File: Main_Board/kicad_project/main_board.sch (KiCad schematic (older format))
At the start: 0 parts

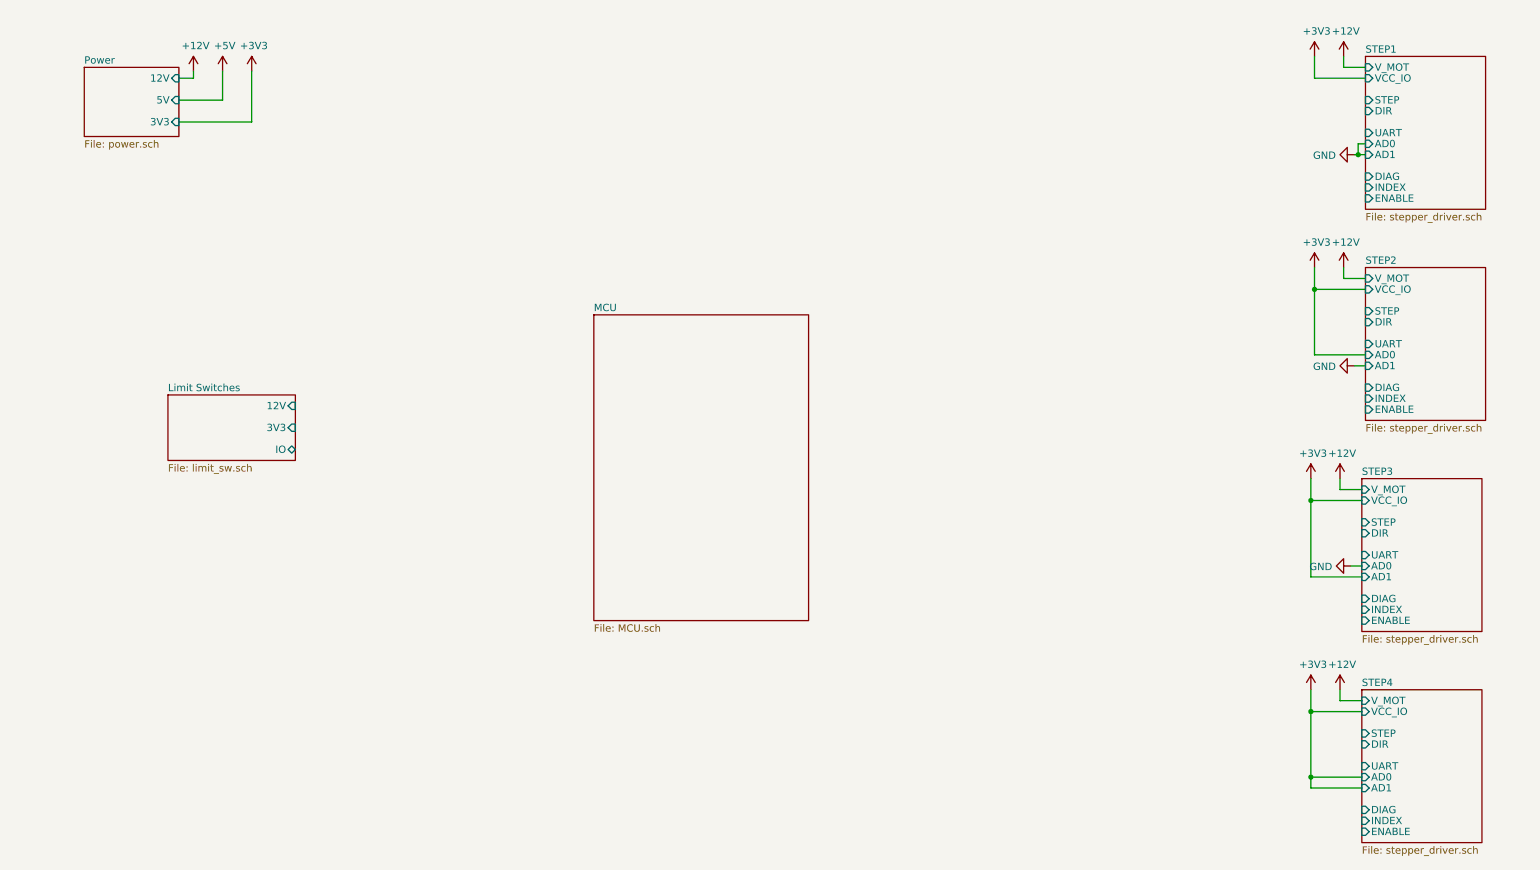
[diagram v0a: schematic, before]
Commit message: add external IO
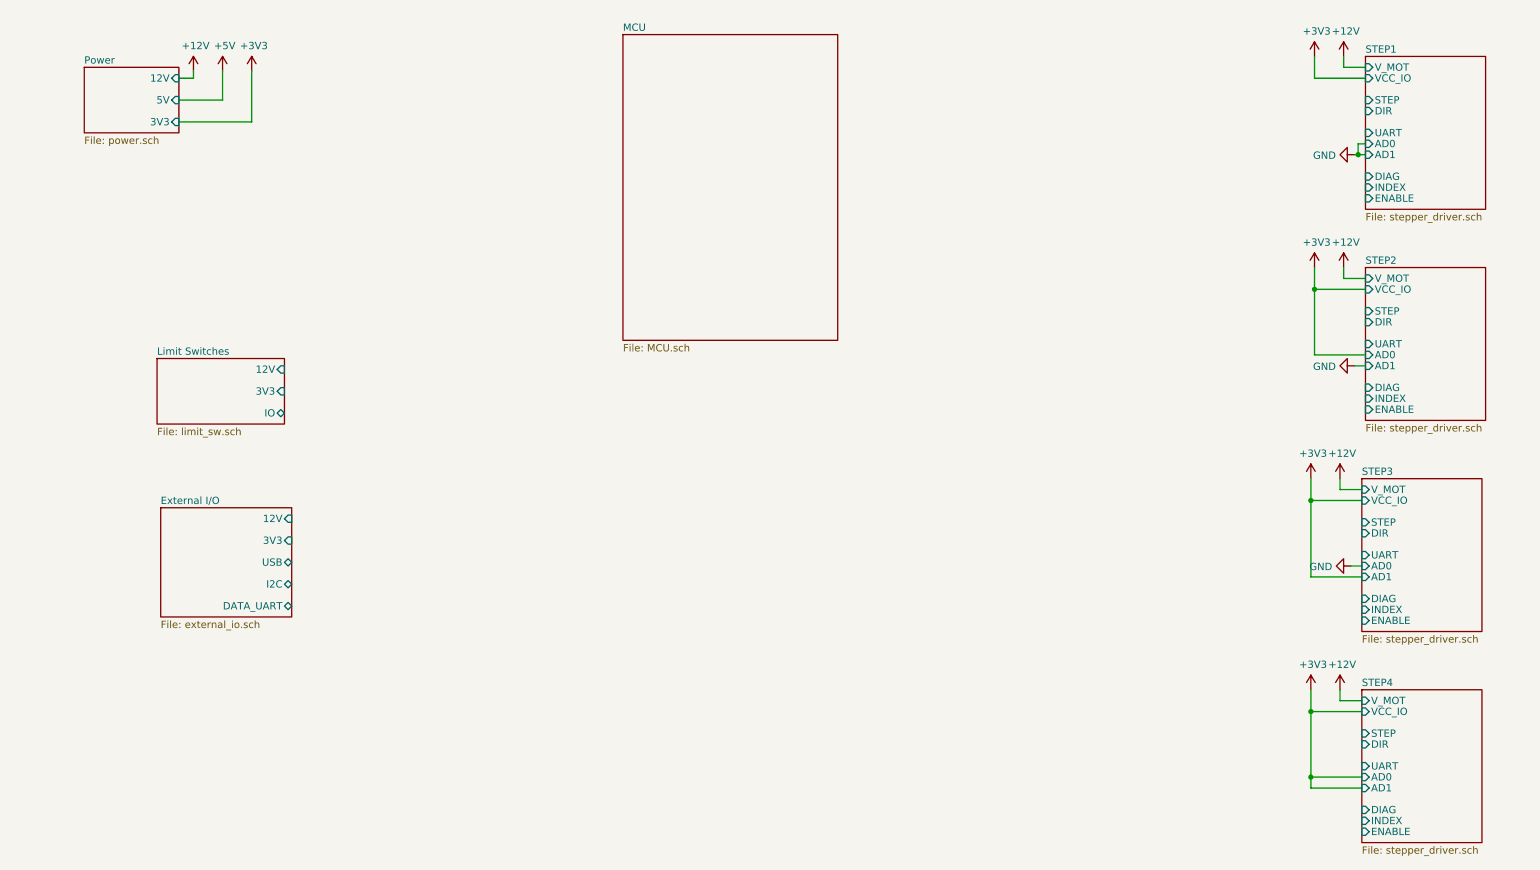
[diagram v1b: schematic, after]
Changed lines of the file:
@@
 $Descr A4 11693 8268
 encoding utf-8
-Sheet 1 8
+Sheet 1 9
 Title "Cube Main Board - top level schematic"
 Date ""
@@
 $EndComp
 $Sheet
-S 1050 925  650  475
+S 1050 925  650  450
 U 5F4D5F3E
 F0 "Power" 50
@@
 $EndComp
 $Sheet
-S 4550 2625 1475 2100
+S 4750 700  1475 2100
 U 5F5463C2
 F0 "MCU" 50
@@
 $EndSheet
 $Sheet
-S 1625 3175 875  450
+S 1550 2925 875  450
 U 5F51A37F
 F0 "Limit Switches" 50
 F1 "limit_sw.sch" 50
-F2 "3V3" I R 2500 3400 50
-F3 "12V" I R 2500 3250 50
-F4 "IO" B R 2500 3550 50
+F2 "3V3" I R 2425 3150 50
+F3 "12V" I R 2425 3000 50
+F4 "IO" B R 2425 3300 50
+$EndSheet
+$Sheet
+S 1575 3950 900  750
+U 5F709561
+F0 "External I/O" 50
+F1 "external_io.sch" 50
+F2 "USB" B R 2475 4325 50
+F3 "3V3" I R 2475 4175 50
+F4 "12V" I R 2475 4025 50
+F5 "I2C" B R 2475 4475 50
+F6 "DATA_UART" B R 2475 4625 50
 $EndSheet
 $EndSCHEMATC

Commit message: progress?
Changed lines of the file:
@@
 	9500 1000 9500 850
 $Comp
-L power:+3V3 #PWR?
+L power:+3V3 #PWR06
 U 1 1 5F4AAFEB
 P 9500 850
-F 0 "#PWR?" H 9500 700 50  0001 C CNN
+F 0 "#PWR06" H 9500 700 50  0001 C CNN
 F 1 "+3V3" H 9515 1023 50  0000 C CNN
 F 2 "" H 9500 850 50  0001 C CNN
@@
 	9500 2450 9500 2300
 $Comp
-L power:+3V3 #PWR?
+L power:+3V3 #PWR07
 U 1 1 5F4AC7A4
 P 9500 2300
-F 0 "#PWR?" H 9500 2150 50  0001 C CNN
+F 0 "#PWR07" H 9500 2150 50  0001 C CNN
 F 1 "+3V3" H 9515 2473 50  0000 C CNN
 F 2 "" H 9500 2300 50  0001 C CNN
@@
 	9475 3900 9475 3750
 $Comp
-L power:+3V3 #PWR?
+L power:+3V3 #PWR04
 U 1 1 5F4AD226
 P 9475 3750
-F 0 "#PWR?" H 9475 3600 50  0001 C CNN
+F 0 "#PWR04" H 9475 3600 50  0001 C CNN
 F 1 "+3V3" H 9490 3923 50  0000 C CNN
 F 2 "" H 9475 3750 50  0001 C CNN
@@
 	9475 5350 9475 5200
 $Comp
-L power:+3V3 #PWR?
+L power:+3V3 #PWR05
 U 1 1 5F4ADFB4
 P 9475 5200
-F 0 "#PWR?" H 9475 5050 50  0001 C CNN
+F 0 "#PWR05" H 9475 5050 50  0001 C CNN
 F 1 "+3V3" H 9490 5373 50  0000 C CNN
 F 2 "" H 9475 5200 50  0001 C CNN
@@
 $EndComp
 $Sheet
-S 1050 925  650  450
+S 1200 925  650  450
 U 5F4D5F3E
 F0 "Power" 50
 F1 "power.sch" 50
-F2 "3V3" I R 1700 1300 50
-F3 "12V" I R 1700 1000 50
-F4 "5V" I R 1700 1150 50
-$EndSheet
-$Comp
-L power:+12V #PWR?
+F2 "3V3" I R 1850 1300 50
+F3 "12V" I R 1850 1000 50
+F4 "5V" I R 1850 1150 50
+$EndSheet
+$Comp
+L power:+12V #PWR09
 U 1 1 5F5780D9
 P 9675 5200
-F 0 "#PWR?" H 9675 5050 50  0001 C CNN
+F 0 "#PWR09" H 9675 5050 50  0001 C CNN
 F 1 "+12V" H 9690 5373 50  0000 C CNN
 F 2 "" H 9675 5200 50  0001 C CNN
@@
 $EndComp
 $Comp
-L power:+12V #PWR?
+L power:+12V #PWR08
 U 1 1 5F578445
 P 9675 3750
-F 0 "#PWR?" H 9675 3600 50  0001 C CNN
+F 0 "#PWR08" H 9675 3600 50  0001 C CNN
 F 1 "+12V" H 9690 3923 50  0000 C CNN
 F 2 "" H 9675 3750 50  0001 C CNN
@@
 $EndComp
 $Comp
-L power:+12V #PWR?
+L power:+12V #PWR011
 U 1 1 5F578DCD
 P 9700 2300
-F 0 "#PWR?" H 9700 2150 50  0001 C CNN
+F 0 "#PWR011" H 9700 2150 50  0001 C CNN
 F 1 "+12V" H 9715 2473 50  0000 C CNN
 F 2 "" H 9700 2300 50  0001 C CNN
@@
 $EndComp
 $Comp
-L power:+12V #PWR?
+L power:+12V #PWR010
 U 1 1 5F579C0A
 P 9700 850
-F 0 "#PWR?" H 9700 700 50  0001 C CNN
+F 0 "#PWR010" H 9700 700 50  0001 C CNN
 F 1 "+12V" H 9715 1023 50  0000 C CNN
 F 2 "" H 9700 850 50  0001 C CNN
@@
 $EndComp
 $Comp
-L power:+12V #PWR?
+L power:+12V #PWR01
 U 1 1 5F634CDC
-P 1800 950
-F 0 "#PWR?" H 1800 800 50  0001 C CNN
-F 1 "+12V" H 1815 1123 50  0000 C CNN
-F 2 "" H 1800 950 50  0001 C CNN
-F 3 "" H 1800 950 50  0001 C CNN
-	1    1800 950
-	1    0    0    -1
-$EndComp
-$Comp
-L power:+3V3 #PWR?
+P 1950 950
+F 0 "#PWR01" H 1950 800 50  0001 C CNN
+F 1 "+12V" H 1965 1123 50  0000 C CNN
+F 2 "" H 1950 950 50  0001 C CNN
+F 3 "" H 1950 950 50  0001 C CNN
+	1    1950 950
+	1    0    0    -1
+$EndComp
+$Comp
+L power:+3V3 #PWR03
 U 1 1 5F635D56
-P 2200 950
-F 0 "#PWR?" H 2200 800 50  0001 C CNN
-F 1 "+3V3" H 2215 1123 50  0000 C CNN
-F 2 "" H 2200 950 50  0001 C CNN
-F 3 "" H 2200 950 50  0001 C CNN
-	1    2200 950
-	1    0    0    -1
-$EndComp
-$Comp
-L power:+5V #PWR?
+P 2350 950
+F 0 "#PWR03" H 2350 800 50  0001 C CNN
+F 1 "+3V3" H 2365 1123 50  0000 C CNN
+F 2 "" H 2350 950 50  0001 C CNN
+F 3 "" H 2350 950 50  0001 C CNN
+	1    2350 950
+	1    0    0    -1
+$EndComp
+$Comp
+L power:+5V #PWR02
 U 1 1 5F636812
-P 2000 950
-F 0 "#PWR?" H 2000 800 50  0001 C CNN
-F 1 "+5V" H 2015 1123 50  0000 C CNN
-F 2 "" H 2000 950 50  0001 C CNN
-F 3 "" H 2000 950 50  0001 C CNN
-	1    2000 950
-	1    0    0    -1
-$EndComp
-Wire Wire Line
-	2200 950  2200 1300
-Wire Wire Line
-	2200 1300 1700 1300
-Wire Wire Line
-	1700 1150 2000 1150
-Wire Wire Line
-	2000 1150 2000 950
-Wire Wire Line
-	1700 1000 1800 1000
-Wire Wire Line
-	1800 1000 1800 950
+P 2150 950
+F 0 "#PWR02" H 2150 800 50  0001 C CNN
+F 1 "+5V" H 2165 1123 50  0000 C CNN
+F 2 "" H 2150 950 50  0001 C CNN
+F 3 "" H 2150 950 50  0001 C CNN
+	1    2150 950
+	1    0    0    -1
+$EndComp
+Wire Wire Line
+	2350 950  2350 1300
+Wire Wire Line
+	2350 1300 1850 1300
+Wire Wire Line
+	1850 1150 2150 1150
+Wire Wire Line
+	2150 1150 2150 950
+Wire Wire Line
+	1850 1000 1950 1000
+Wire Wire Line
+	1950 1000 1950 950
 Wire Wire Line
 	9825 4425 9475 4425
@@
 Connection ~ 9475 5800
 $Comp
-L power:GND #PWR?
+L power:GND #PWR013
 U 1 1 5F537589
 P 9775 1525
-F 0 "#PWR?" H 9775 1275 50  0001 C CNN
+F 0 "#PWR013" H 9775 1275 50  0001 C CNN
 F 1 "GND" V 9780 1397 50  0000 R CNN
 F 2 "" H 9775 1525 50  0001 C CNN
@@
 $EndComp
 $Comp
-L power:GND #PWR?
+L power:GND #PWR014
 U 1 1 5F53878C
 P 9775 2975
-F 0 "#PWR?" H 9775 2725 50  0001 C CNN
+F 0 "#PWR014" H 9775 2725 50  0001 C CNN
 F 1 "GND" V 9780 2847 50  0000 R CNN
 F 2 "" H 9775 2975 50  0001 C CNN
@@
 	9500 2900 9500 2450
 $Comp
-L power:GND #PWR?
+L power:GND #PWR012
 U 1 1 5F5393A9
 P 9750 4350
-F 0 "#PWR?" H 9750 4100 50  0001 C CNN
+F 0 "#PWR012" H 9750 4100 50  0001 C CNN
 F 1 "GND" V 9755 4222 50  0000 R CNN
 F 2 "" H 9750 4350 50  0001 C CNN
@@
 $EndComp
 $Sheet
-S 4750 700  1475 2100
+S 5225 2475 1475 2100
 U 5F5463C2
 F0 "MCU" 50
 F1 "MCU.sch" 50
-$EndSheet
-$Sheet
-S 1550 2925 875  450
+F2 "VDD" I L 5225 2575 50
+F3 "VDDA" I L 5225 2700 50
+F4 "USB" B L 5225 3275 50
+$EndSheet
+$Sheet
+S 3000 2550 875  450
 U 5F51A37F
 F0 "Limit Switches" 50
 F1 "limit_sw.sch" 50
-F2 "3V3" I R 2425 3150 50
-F3 "12V" I R 2425 3000 50
-F4 "IO" B R 2425 3300 50
-$EndSheet
-$Sheet
-S 1575 3950 900  750
+F2 "3V3" I R 3875 2775 50
+F3 "12V" I R 3875 2625 50
+F4 "IO" B R 3875 2925 50
+$EndSheet
+$Sheet
+S 3000 3275 900  750
 U 5F709561
 F0 "External I/O" 50
 F1 "external_io.sch" 50
-F2 "USB" B R 2475 4325 50
-F3 "3V3" I R 2475 4175 50
-F4 "12V" I R 2475 4025 50
-F5 "I2C" B R 2475 4475 50
-F6 "DATA_UART" B R 2475 4625 50
-$EndSheet
+F2 "USB" B R 3900 3650 50
+F3 "3V3" I R 3900 3500 50
+F4 "12V" I R 3900 3350 50
+F5 "I2C" B R 3900 3800 50
+F6 "DATA_UART" B R 3900 3950 50
+$EndSheet
+Wire Bus Line
+	3900 3650 4550 3650
+Wire Bus Line
+	4550 3650 4550 3275
+Wire Bus Line
+	4550 3275 5225 3275
 $EndSCHEMATC

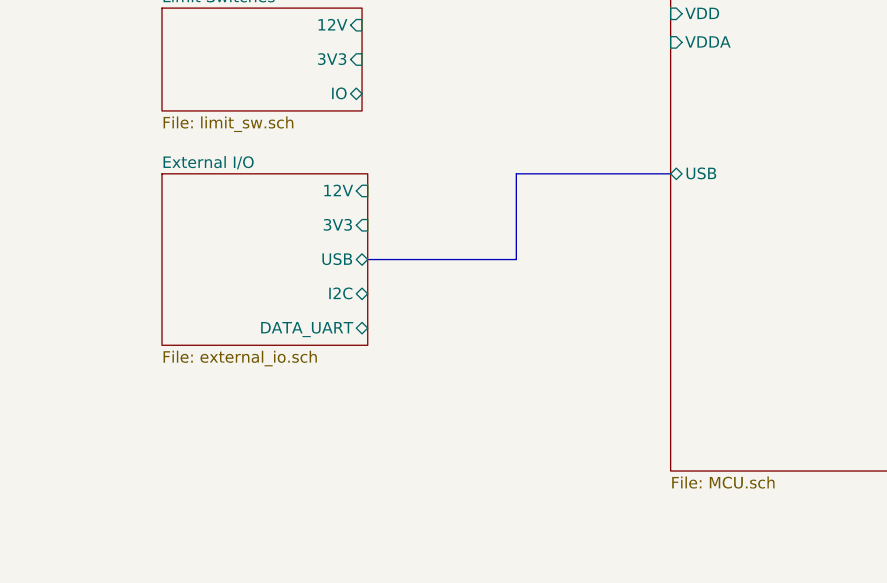
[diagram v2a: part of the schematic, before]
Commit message: progress on MCU pinout
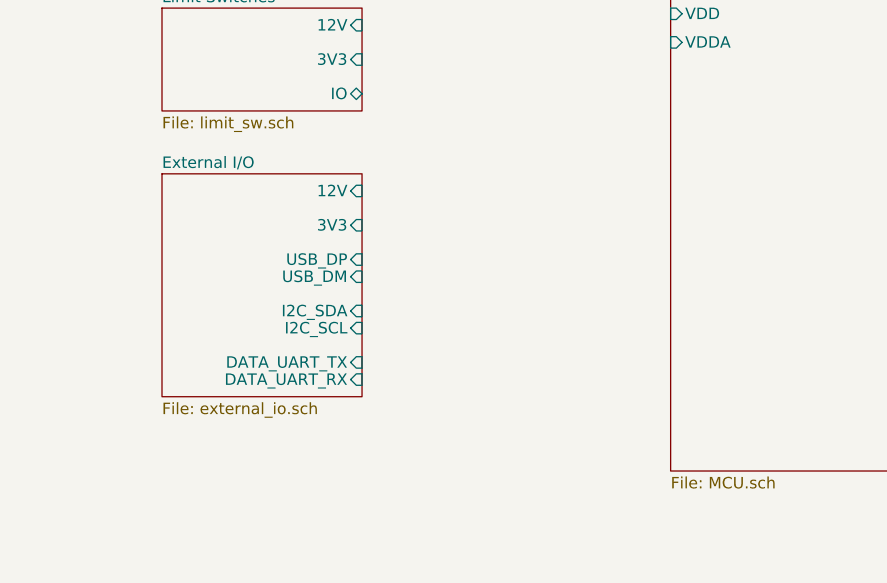
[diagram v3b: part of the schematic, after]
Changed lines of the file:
@@
 	9500 1000 9500 850
 $Comp
-L power:+3V3 #PWR06
+L power:+3V3 #PWR?
 U 1 1 5F4AAFEB
 P 9500 850
-F 0 "#PWR06" H 9500 700 50  0001 C CNN
+F 0 "#PWR?" H 9500 700 50  0001 C CNN
 F 1 "+3V3" H 9515 1023 50  0000 C CNN
 F 2 "" H 9500 850 50  0001 C CNN
@@
 	9500 2450 9500 2300
 $Comp
-L power:+3V3 #PWR07
+L power:+3V3 #PWR?
 U 1 1 5F4AC7A4
 P 9500 2300
-F 0 "#PWR07" H 9500 2150 50  0001 C CNN
+F 0 "#PWR?" H 9500 2150 50  0001 C CNN
 F 1 "+3V3" H 9515 2473 50  0000 C CNN
 F 2 "" H 9500 2300 50  0001 C CNN
@@
 	9475 3900 9475 3750
 $Comp
-L power:+3V3 #PWR04
+L power:+3V3 #PWR?
 U 1 1 5F4AD226
 P 9475 3750
-F 0 "#PWR04" H 9475 3600 50  0001 C CNN
+F 0 "#PWR?" H 9475 3600 50  0001 C CNN
 F 1 "+3V3" H 9490 3923 50  0000 C CNN
 F 2 "" H 9475 3750 50  0001 C CNN
@@
 	9475 5350 9475 5200
 $Comp
-L power:+3V3 #PWR05
+L power:+3V3 #PWR?
 U 1 1 5F4ADFB4
 P 9475 5200
-F 0 "#PWR05" H 9475 5050 50  0001 C CNN
+F 0 "#PWR?" H 9475 5050 50  0001 C CNN
 F 1 "+3V3" H 9490 5373 50  0000 C CNN
 F 2 "" H 9475 5200 50  0001 C CNN
@@
 $EndSheet
 $Comp
-L power:+12V #PWR09
+L power:+12V #PWR?
 U 1 1 5F5780D9
 P 9675 5200
-F 0 "#PWR09" H 9675 5050 50  0001 C CNN
+F 0 "#PWR?" H 9675 5050 50  0001 C CNN
 F 1 "+12V" H 9690 5373 50  0000 C CNN
 F 2 "" H 9675 5200 50  0001 C CNN
@@
 $EndComp
 $Comp
-L power:+12V #PWR08
+L power:+12V #PWR?
 U 1 1 5F578445
 P 9675 3750
-F 0 "#PWR08" H 9675 3600 50  0001 C CNN
+F 0 "#PWR?" H 9675 3600 50  0001 C CNN
 F 1 "+12V" H 9690 3923 50  0000 C CNN
 F 2 "" H 9675 3750 50  0001 C CNN
@@
 $EndComp
 $Comp
-L power:+12V #PWR011
+L power:+12V #PWR?
 U 1 1 5F578DCD
 P 9700 2300
-F 0 "#PWR011" H 9700 2150 50  0001 C CNN
+F 0 "#PWR?" H 9700 2150 50  0001 C CNN
 F 1 "+12V" H 9715 2473 50  0000 C CNN
 F 2 "" H 9700 2300 50  0001 C CNN
@@
 $EndComp
 $Comp
-L power:+12V #PWR010
+L power:+12V #PWR?
 U 1 1 5F579C0A
 P 9700 850
-F 0 "#PWR010" H 9700 700 50  0001 C CNN
+F 0 "#PWR?" H 9700 700 50  0001 C CNN
 F 1 "+12V" H 9715 1023 50  0000 C CNN
 F 2 "" H 9700 850 50  0001 C CNN
@@
 $EndComp
 $Comp
-L power:+12V #PWR01
+L power:+12V #PWR?
 U 1 1 5F634CDC
 P 1950 950
-F 0 "#PWR01" H 1950 800 50  0001 C CNN
+F 0 "#PWR?" H 1950 800 50  0001 C CNN
 F 1 "+12V" H 1965 1123 50  0000 C CNN
 F 2 "" H 1950 950 50  0001 C CNN
@@
 $EndComp
 $Comp
-L power:+3V3 #PWR03
+L power:+3V3 #PWR?
 U 1 1 5F635D56
 P 2350 950
-F 0 "#PWR03" H 2350 800 50  0001 C CNN
+F 0 "#PWR?" H 2350 800 50  0001 C CNN
 F 1 "+3V3" H 2365 1123 50  0000 C CNN
 F 2 "" H 2350 950 50  0001 C CNN
@@
 $EndComp
 $Comp
-L power:+5V #PWR02
+L power:+5V #PWR?
 U 1 1 5F636812
 P 2150 950
-F 0 "#PWR02" H 2150 800 50  0001 C CNN
+F 0 "#PWR?" H 2150 800 50  0001 C CNN
 F 1 "+5V" H 2165 1123 50  0000 C CNN
 F 2 "" H 2150 950 50  0001 C CNN
@@
 Connection ~ 9475 5800
 $Comp
-L power:GND #PWR013
+L power:GND #PWR?
 U 1 1 5F537589
 P 9775 1525
-F 0 "#PWR013" H 9775 1275 50  0001 C CNN
+F 0 "#PWR?" H 9775 1275 50  0001 C CNN
 F 1 "GND" V 9780 1397 50  0000 R CNN
 F 2 "" H 9775 1525 50  0001 C CNN
@@
 $EndComp
 $Comp
-L power:GND #PWR014
+L power:GND #PWR?
 U 1 1 5F53878C
 P 9775 2975
-F 0 "#PWR014" H 9775 2725 50  0001 C CNN
+F 0 "#PWR?" H 9775 2725 50  0001 C CNN
 F 1 "GND" V 9780 2847 50  0000 R CNN
 F 2 "" H 9775 2975 50  0001 C CNN
@@
 	9500 2900 9500 2450
 $Comp
-L power:GND #PWR012
+L power:GND #PWR?
 U 1 1 5F5393A9
 P 9750 4350
-F 0 "#PWR012" H 9750 4100 50  0001 C CNN
+F 0 "#PWR?" H 9750 4100 50  0001 C CNN
 F 1 "GND" V 9755 4222 50  0000 R CNN
 F 2 "" H 9750 4350 50  0001 C CNN
@@
 F2 "VDD" I L 5225 2575 50
 F3 "VDDA" I L 5225 2700 50
-F4 "USB" B L 5225 3275 50
 $EndSheet
 $Sheet
@@
 $EndSheet
 $Sheet
-S 3000 3275 900  750
+S 3000 3275 875  975
 U 5F709561
 F0 "External I/O" 50
 F1 "external_io.sch" 50
-F2 "USB" B R 3900 3650 50
-F3 "3V3" I R 3900 3500 50
-F4 "12V" I R 3900 3350 50
-F5 "I2C" B R 3900 3800 50
-F6 "DATA_UART" B R 3900 3950 50
-$EndSheet
-Wire Bus Line
-	3900 3650 4550 3650
-Wire Bus Line
-	4550 3650 4550 3275
-Wire Bus Line
-	4550 3275 5225 3275
+F2 "3V3" I R 3875 3500 50
+F3 "12V" I R 3875 3350 50
+F4 "USB_DP" I R 3875 3650 50
+F5 "USB_DM" I R 3875 3725 50
+F6 "I2C_SDA" I R 3875 3875 50
+F7 "I2C_SCL" I R 3875 3950 50
+F8 "DATA_UART_TX" I R 3875 4100 50
+F9 "DATA_UART_RX" I R 3875 4175 50
+$EndSheet
 $EndSCHEMATC

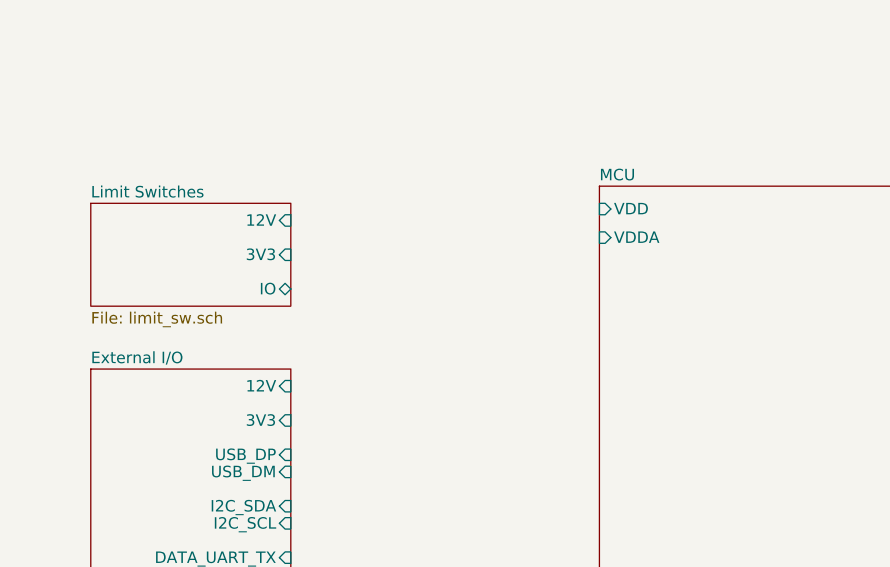
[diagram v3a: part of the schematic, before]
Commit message: fix bus connection
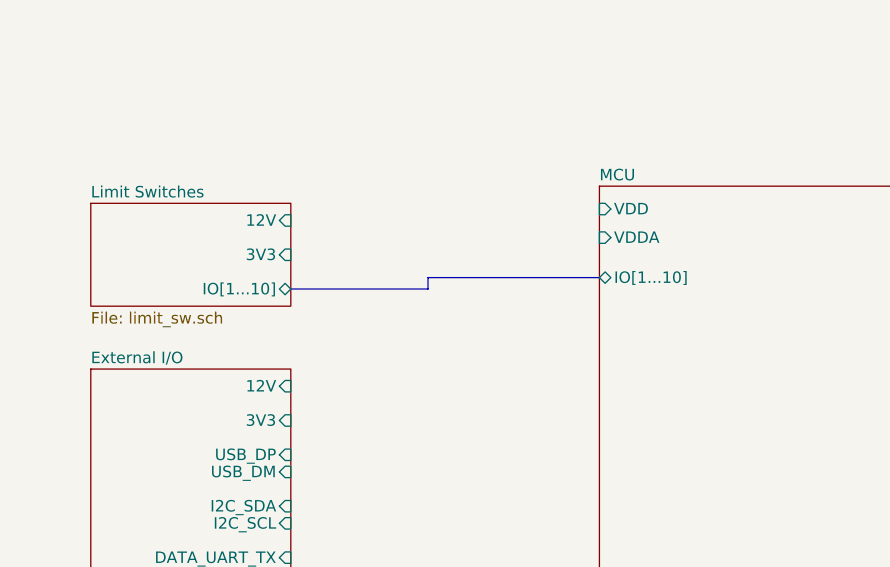
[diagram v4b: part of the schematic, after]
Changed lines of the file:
@@
 $EndComp
-$Sheet
-S 5225 2475 1475 2100
-U 5F5463C2
-F0 "MCU" 50
-F1 "MCU.sch" 50
-F2 "VDD" I L 5225 2575 50
-F3 "VDDA" I L 5225 2700 50
-$EndSheet
-$Sheet
-S 3000 2550 875  450
-U 5F51A37F
-F0 "Limit Switches" 50
-F1 "limit_sw.sch" 50
-F2 "3V3" I R 3875 2775 50
-F3 "12V" I R 3875 2625 50
-F4 "IO" B R 3875 2925 50
-$EndSheet
 $Sheet
 S 3000 3275 875  975
@@
 F9 "DATA_UART_RX" I R 3875 4175 50
 $EndSheet
+$Sheet
+S 5225 2475 1475 2100
+U 5F5463C2
+F0 "MCU" 50
+F1 "MCU.sch" 50
+F2 "VDD" I L 5225 2575 50
+F3 "VDDA" I L 5225 2700 50
+F4 "IO[1...10]" B L 5225 2875 50
+$EndSheet
+$Sheet
+S 3000 2550 875  450
+U 5F51A37F
+F0 "Limit Switches" 50
+F1 "limit_sw.sch" 50
+F2 "3V3" I R 3875 2775 50
+F3 "12V" I R 3875 2625 50
+F4 "IO[1...10]" B R 3875 2925 50
+$EndSheet
+Wire Bus Line
+	3875 2925 4475 2925
+Wire Bus Line
+	4475 2925 4475 2875
+Wire Bus Line
+	4475 2875 5225 2875
 $EndSCHEMATC
